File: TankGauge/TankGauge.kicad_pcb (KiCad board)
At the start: 4 copper layers, 42.5 x 44.5 mm, 20 parts, among them J1 Screw_Terminal_01x02, J2 Screw_Terminal_01x04, J3 Screw_Terminal_01x02, J4 Screw_Terminal_01x03, Q1 IRF540N, U1 LTC4365TS8, U2 TMP100

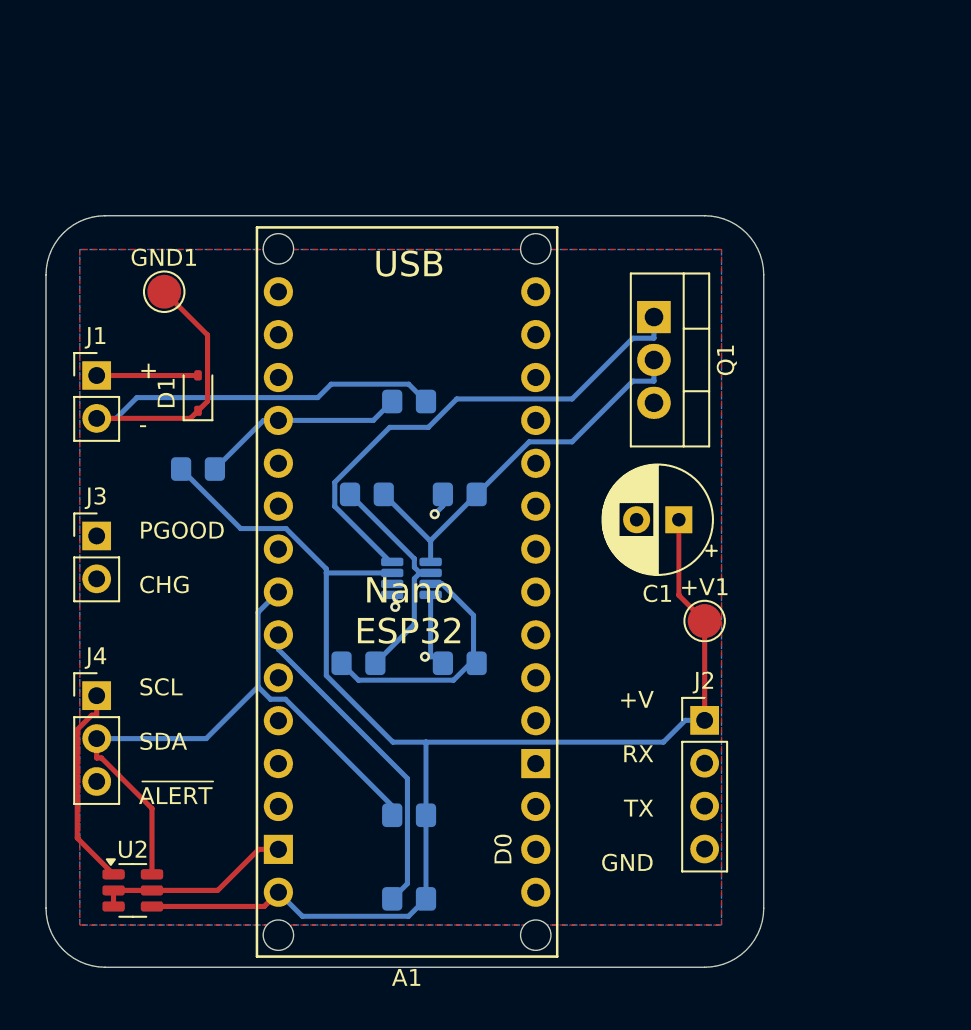
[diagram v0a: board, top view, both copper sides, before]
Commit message: Use the eTape and a ADS1115 for better results.
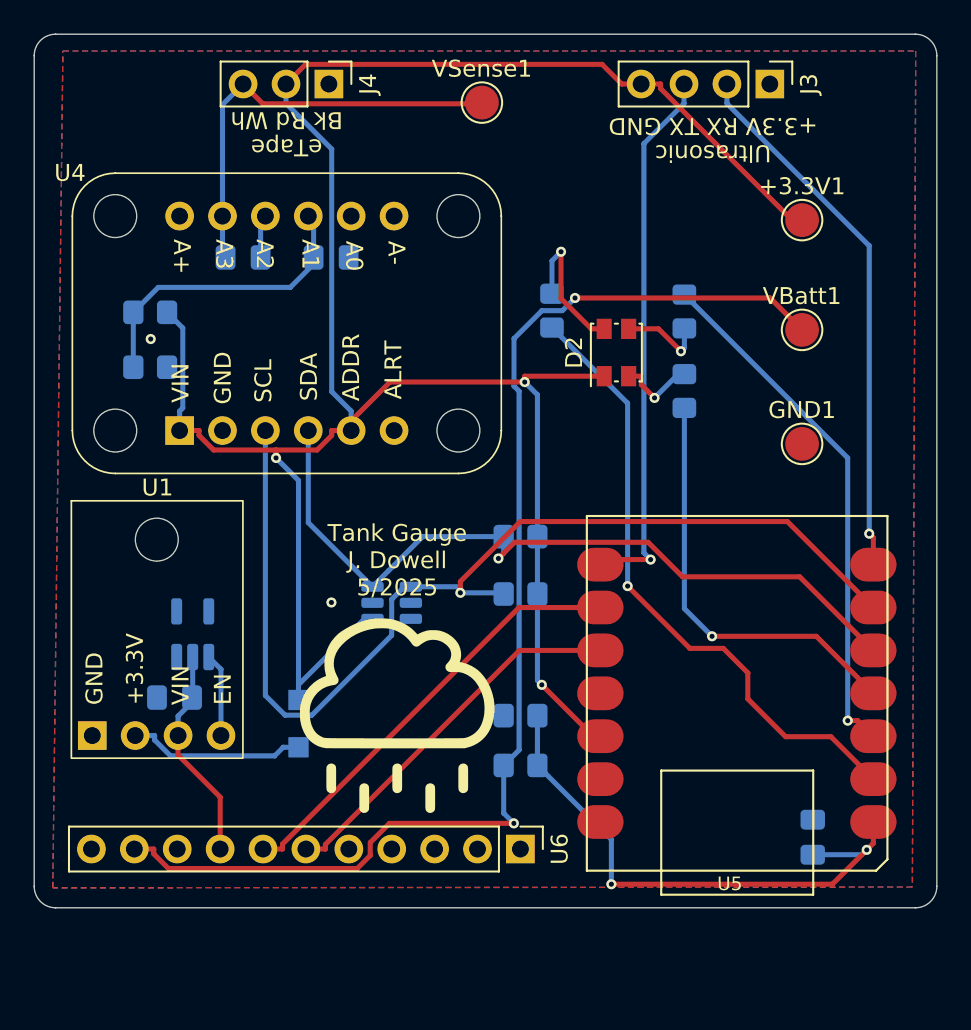
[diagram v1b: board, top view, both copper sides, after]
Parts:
- removed +V1: TestPoint, TestPoint:TestPoint_Pad_D2.0mm
- removed A1: Arduino_Nano_33_BLE_Socket, PCM_arduino-library:Arduino_Nano_Every_Socket
- removed J1: Screw_Terminal_01x02, Connector_PinHeader_2.54mm:PinHeader_1x02_P2.54mm_Vertical
- removed J2: Screw_Terminal_01x04, Connector_PinHeader_2.54mm:PinHeader_1x04_P2.54mm_Vertical
- removed Q1: IRF540N, Package_TO_SOT_THT:TO-220-3_Vertical
- added +3.3V1: TestPoint, TestPoint:TestPoint_Pad_D2.0mm, F.Cu at (128.3, 57.8)
- added C2: 0.1uF, Capacitor_SMD:C_0805_2012Metric_Pad1.18x1.45mm_HandSolder, B.Cu at (100.4, 60.0)
- added C3: 0.1uF, Capacitor_SMD:C_0805_2012Metric_Pad1.18x1.45mm_HandSolder, B.Cu at (95.2, 60.0)
- added C4: 0.1uF, Capacitor_SMD:C_0805_2012Metric_Pad1.18x1.45mm_HandSolder, B.Cu at (128.9, 94.3)
- added D2: LED_ARGB, LED_SMD:LED_Kingbright_AAA3528ESGCT, F.Cu at (117.3, 65.6)
- added G1: LOGO, Symbol:RainCache, F.Cu at (104.3, 87.1)
- added R9: 10k, Resistor_SMD:R_0805_2012Metric_Pad1.20x1.40mm_HandSolder, B.Cu at (111.6, 79.9)
- added U3: TMP100, Package_TO_SOT_SMD:SOT-23-6, B.Cu at (104.0, 80.4)
- added U4: ~, Module:ADS1115 Breakout Board, F.Cu at (85.1, 55.0)
- added U5: MOUDLE-SEEEDUINO-XIAO-ESP32C3, Library:XIAO-ESP32C3, F.Cu at (133.3, 75.3)
- added U6: BQ24074, Connector_PinHeader_2.54mm:PinHeader_1x11_P2.54mm_Vertical, F.Cu at (111.6, 95.0)
- added VBatt1: TestPoint, TestPoint:TestPoint_Pad_D2.0mm, F.Cu at (128.3, 64.3)
- added VSense1: TestPoint, TestPoint:TestPoint_Pad_D2.0mm, F.Cu at (109.3, 50.8)
- C1: value 100uF -> 1uF; footprint Capacitor_THT:CP_Radial_D6.3mm_P2.50mm -> Capacitor_SMD:C_0805_2012Metric_Pad1.18x1.45mm_HandSolder; moved to B.Cu
- D1: value SD12_SOD323 -> PMEG6020AELRX; footprint Diode_SMD:D_SOD-323 -> Diode_SMD:Nexperia_CFP3_SOD-123W; moved to B.Cu
- J3: value Screw_Terminal_01x02 -> Ultrasonic; footprint Connector_PinHeader_2.54mm:PinHeader_1x02_P2.54mm_Vertical -> Connector_PinHeader_2.54mm:PinHeader_1x04_P2.54mm_Vertical
- J4: value Screw_Terminal_01x03 -> eTape
- R1: value 215k -> 10k
- R2: value 84.5k -> 30k
- R3: value 1.91M -> 1.8k
- R4: value 100k -> 1.8k
- R5: value 10k -> 1.8k
- R7: value 47k -> 30k
- R8: value 84.5k -> 10k
- U1: value LTC4365TS8 -> TLV62569; footprint Package_TO_SOT_SMD:TSOT-23-8 -> Module:TLV62569 Breakout Board; moved to F.Cu
- U2: value TMP100 -> TPS3840DL37; footprint Package_TO_SOT_SMD:SOT-23-6 -> Package_TO_SOT_SMD:SOT-23-5_HandSoldering; moved to B.Cu
- moved J3 48.0 mm to (126.4, 49.7), turned to -90 degrees
- moved GND1 38.8 mm to (128.3, 71.0)
- moved J4 38.7 mm to (100.2, 49.7), turned to -90 degrees
- moved C1 31.7 mm to (91.1, 86.0)
- moved R5 29.9 mm to (121.3, 67.9), turned to -90 degrees
- moved R1 27.7 mm to (89.7, 63.2)
- moved R7 24.0 mm to (111.6, 87.1), turned to 180 degrees
- moved R2 21.4 mm to (89.7, 66.5), turned to 0 degrees
- moved D1 20.5 mm to (98.4, 87.6), turned to -90 degrees
- moved R4 17.2 mm to (121.3, 63.2), turned to 90 degrees
- moved U2 15.6 mm to (92.2, 82.3), turned to 90 degrees
- moved R3 15.4 mm to (113.5, 63.1), turned to -90 degrees
- moved U1 15.4 mm to (90.1, 82.0), turned to 0 degrees
- moved R8 10.4 mm to (111.6, 76.5), turned to 180 degrees
- moved R6 10.3 mm to (111.6, 90.0), turned to 0 degrees
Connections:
- C1 pad 1: VOUT -> VREG
- D1 pad 1: GND -> +3.3V
- D1 pad 2: VIN -> Net-(D1-A)
- J3 pad 1: PGOOD -> GND
- J3 pad 2: CHG -> TX
- J4 pad 1: SCL -> GND
- J4 pad 2: SDA -> +3.3V
- J4 pad 3: !ALERT -> VLEVEL
- R1 pad 1: Net-(U1-OV) -> +3.3V
- R1 pad 2: GND -> VREF
- R2 pad 1: Net-(U1-UV) -> VREF
- R2 pad 2: Net-(U1-OV) -> GND
- R3 pad 1: VIN -> Net-(D2-RK)
- R3 pad 2: Net-(U1-UV) -> Red
- R4 pad 1: VIN -> Net-(D2-GK)
- R4 pad 2: Net-(U1-~{SHDN}) -> Green
- R5 pad 1: VOUT -> Net-(D2-BK)
- R5 pad 2: SDA -> Blue
- R6 pad 1: VOUT -> LiPo
- R6 pad 2: SCL -> VMON
- R7 pad 1: VOUT -> VMON
- R7 pad 2: VMON -> GND
- R8 pad 1: VMON -> +3.3V
- R8 pad 2: GND -> SDA
- U1 pad 1: VIN -> GND
- U1 pad 2: Net-(U1-UV) -> Net-(D1-A)
- U1 pad 3: Net-(U1-OV) -> VREG
- U1 pad 4: GND -> EN
- U2 pad 1: SCL -> EN
- U2 pad 2: GND -> VREG
- U2 pad 4: VOUT -> unconnected-(U2-!MR/NC-Pad4)
- U2 pad 5: GND -> unconnected-(U2-CT-Pad5)
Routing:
- net +3.3V: track 0.00 -> 137.6 mm, vias 0 -> 3
- net GND: track 136.1 -> 2.57 mm, vias 1 -> 2
- net VOUT: track 92.7 -> 0.00 mm
- net LiPo: track 0.00 -> 73.0 mm, vias 0 -> 2
- net VIN: track 63.1 -> 0.00 mm
- net Red: track 0.00 -> 37.4 mm, vias 0 -> 1
- net !ALERT: track 36.3 -> 0.00 mm
- net Green: track 0.00 -> 31.1 mm, vias 0 -> 1
- net Net-(Q1-G): track 29.9 -> 0.00 mm
- net VLEVEL: track 0.00 -> 25.5 mm
- net Blue: track 0.00 -> 25.2 mm, vias 0 -> 1
- net VMON: track 12.2 -> 32.9 mm, vias 0 -> 2
- net RX: track 12.1 -> 32.4 mm, vias 0 -> 1
- net SCL: track 43.5 -> 63.8 mm, vias 0 -> 1
- net TX: track 12.1 -> 32.1 mm, vias 0 -> 1
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- removed copper zone on In1.Cu, net GND
- removed copper zone on In2.Cu, net GND
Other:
- board size 42.5 x 44.5 mm -> 53.5 x 51.7 mm
- copper layers 4 -> 2
- board text added: "Tank Gauge J. Dowell 5/2025"
- board text added: "Ultrasonic +3.3V RX TX GND"
- board text added: "eTape Bk Rd Wh"
- board text removed: "+ -"
- board text removed: "+V RX TX GND"
- board text removed: "BQ24074"
- board text removed: "JLCJLCJLCJLC"
- board text removed: "MAX17048"
- board text removed: "PGOOD CHG"
- board text removed: "SCL SDA ALERT"
- board text removed: "SEN0208"
- board text removed: "Tank Gauge v2 J. Dowell 3/25"
- board text removed: "USB Nano ESP32"

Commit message: Change voltage divider ratio on the battery monitor.
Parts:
- R6: value 10k -> 30k
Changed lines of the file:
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@@
 			)
 		)
-		(property "Value" "10k"
+		(property "Value" "30k"
 			(at 0 -1.65 0)
 			(layer "B.Fab")
